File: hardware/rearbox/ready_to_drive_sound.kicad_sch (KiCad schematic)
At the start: 4 parts, among them Q6 BUK6D210

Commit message: Changed power section
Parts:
- gave numbers to parts that had none: 1
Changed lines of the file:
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@@
 (kicad_sch
-	(version 20231120)
+	(version 20250114)
 	(generator "eeschema")
-	(generator_version "8.0")
+	(generator_version "9.0")
 	(paper "A4")
 	(title_block
@@
 		(comment 1 "Reviewer:")
 	)
+	(text "+24V"
+		(exclude_from_sim no)
+		(at 161.163 84.709 0)
+		(effects
+			(font
+				(size 1.27 1.27)
+			)
+			(justify left bottom)
+		)
+	)
+	(text "Buzzer"
+		(exclude_from_sim no)
+		(at 164.465 97.536 90)
+		(effects
+			(font
+				(size 1.27 1.27)
+			)
+			(justify left bottom)
+		)
+	)
 	(junction
 		(at 138.43 107.95)
@@
 		)
 	)
-	(text "+24V"
-		(exclude_from_sim no)
-		(at 161.163 84.709 0)
-		(effects
-			(font
-				(size 1.27 1.27)
-			)
-			(justify left bottom)
-		)
-	)
-	(text "Buzzer"
-		(exclude_from_sim no)
-		(at 164.465 97.536 90)
-		(effects
-			(font
-				(size 1.27 1.27)
-			)
-			(justify left bottom)
-		)
-	)
 	(hierarchical_label "IN"
 		(shape input)
 		(at 128.27 107.95 180)
-		(fields_autoplaced yes)
 		(effects
 			(font
@@
 		(shape output)
 		(at 151.13 100.33 0)
-		(fields_autoplaced yes)
 		(effects
 			(font
@@
 		(on_board yes)
 		(dnp no)
-		(property "Reference" "R?"
+		(property "Reference" "R34"
 			(at 143.51 113.03 90)
 			(effects

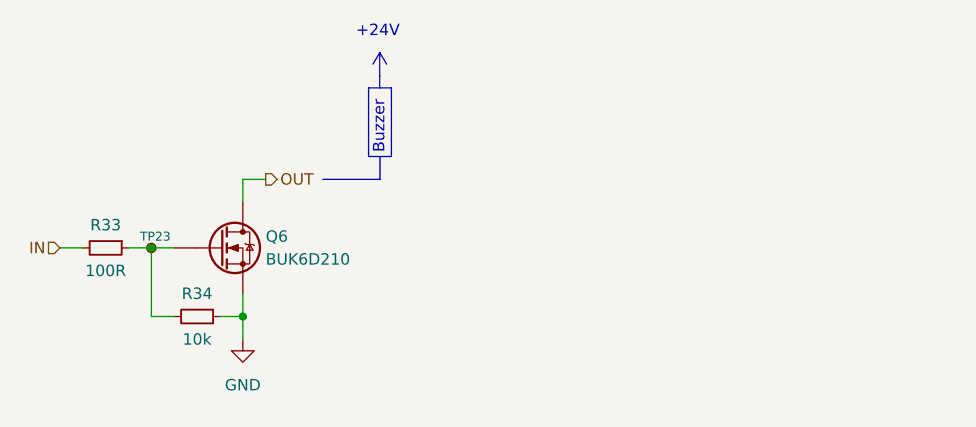
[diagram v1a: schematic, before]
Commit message: Added an auxillary RTDS transistor as a backup
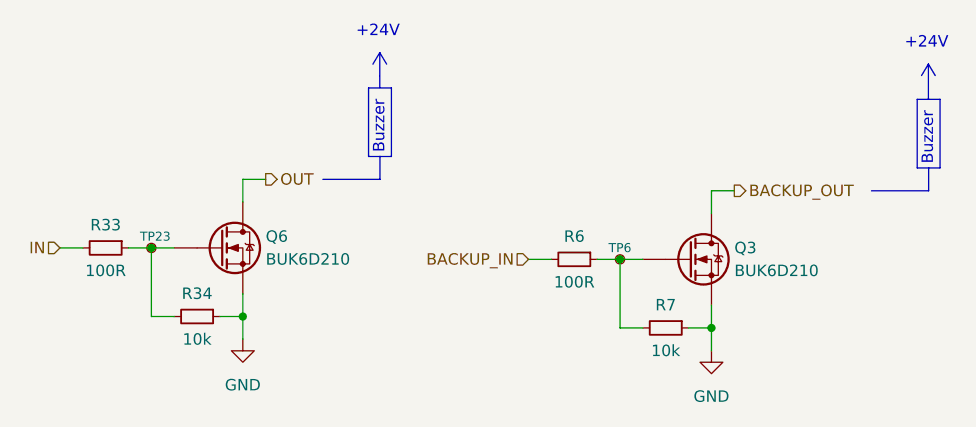
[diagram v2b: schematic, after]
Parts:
- added Q3: BUK6D210, Local_Library:Diodes_UDFN2020-6_Type-F, symbol BUK6D210:BUK6D210
- added R6: 100R, Resistor_SMD:R_0603_1608Metric, symbol Device:R_Small
- added R7: 10k, Resistor_SMD:R_0603_1608Metric, symbol Device:R_Small
- added TP6: TestPoint_Small, TestPoint:TestPoint_Pad_D1.0mm, symbol Connector:TestPoint_Small
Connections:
- net GND: now also Q3.4 (S), Q3.8 (S), R7.1
- new net: Q3.3 (G), R6.1, R7.2, TP6.1
- new net BACKUP_IN: R6.2
- new net BACKUP_OUT: Q3.1 (D), Q3.2 (D), Q3.5 (D), Q3.6 (D), Q3.7 (D)
